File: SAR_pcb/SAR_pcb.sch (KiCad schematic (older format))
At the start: 32 parts, among them J1 Conn_Coaxial_Power, J10 Conn_Coaxial, J2 Conn_Coaxial_Power, J3 Conn_02x10_Top_Bottom, J4 Conn_01x06, J9 Conn_Coaxial, SW1 SW_Push, U2 10B_SAR

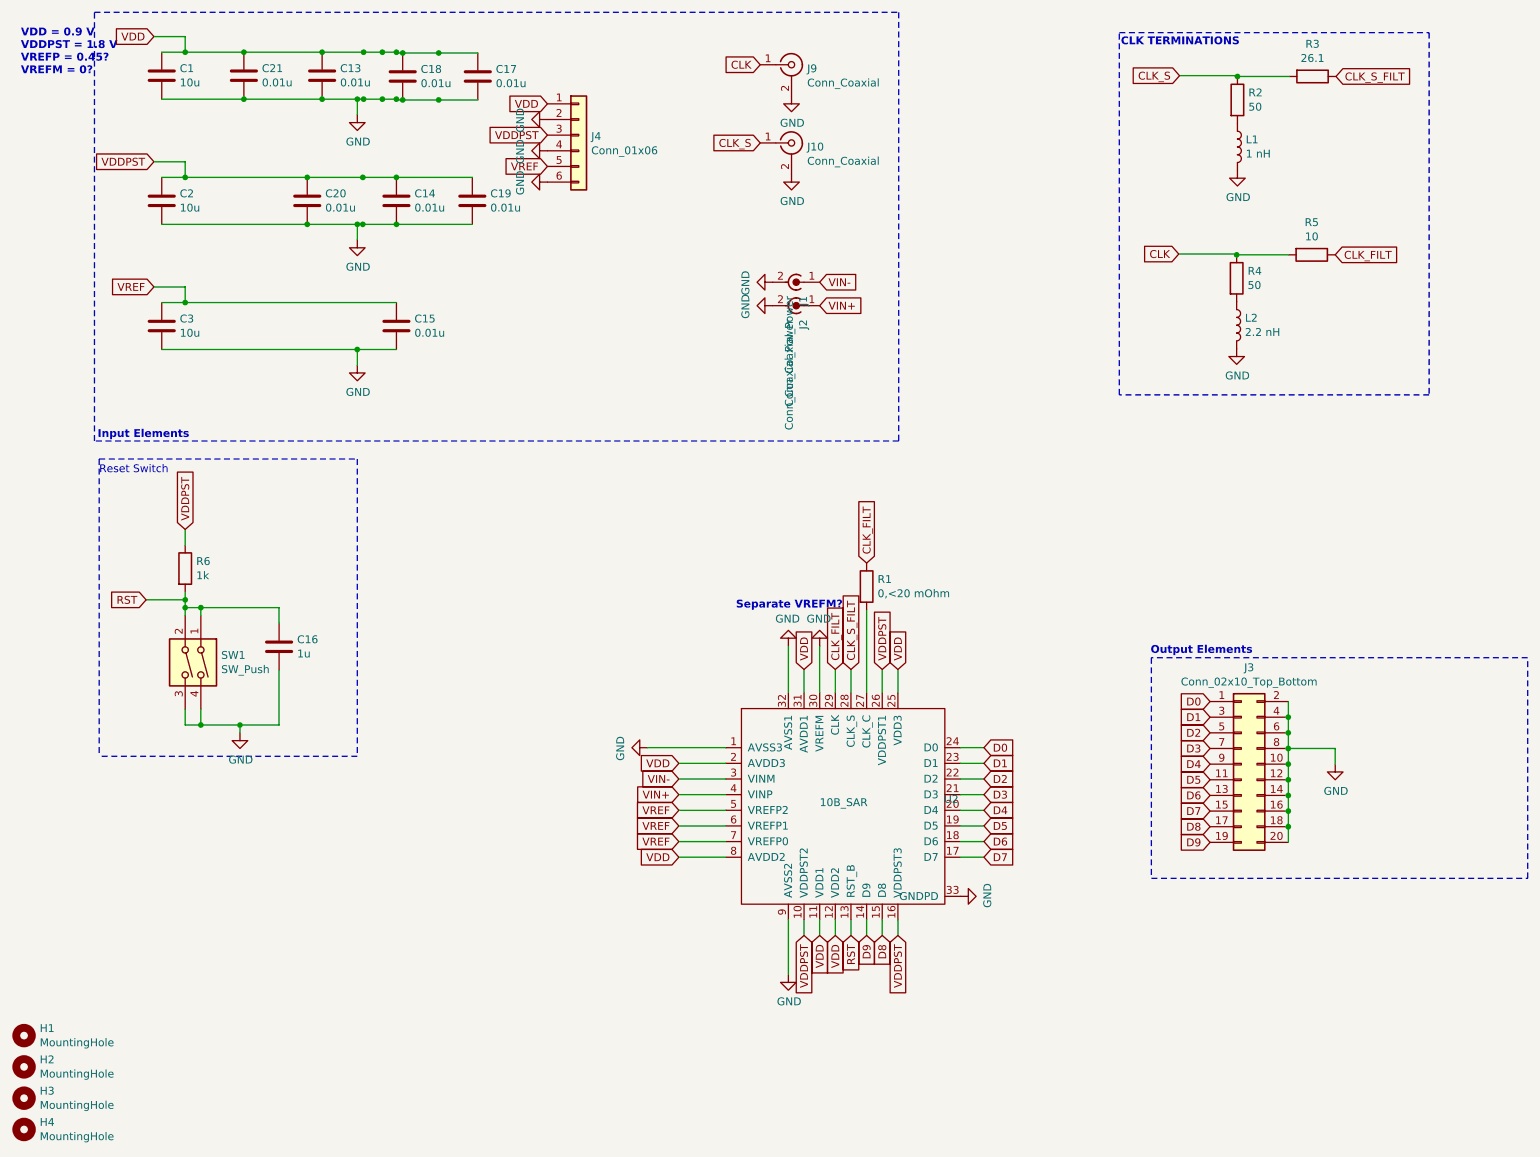
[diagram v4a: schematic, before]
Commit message: Updated BOM for 0603 components
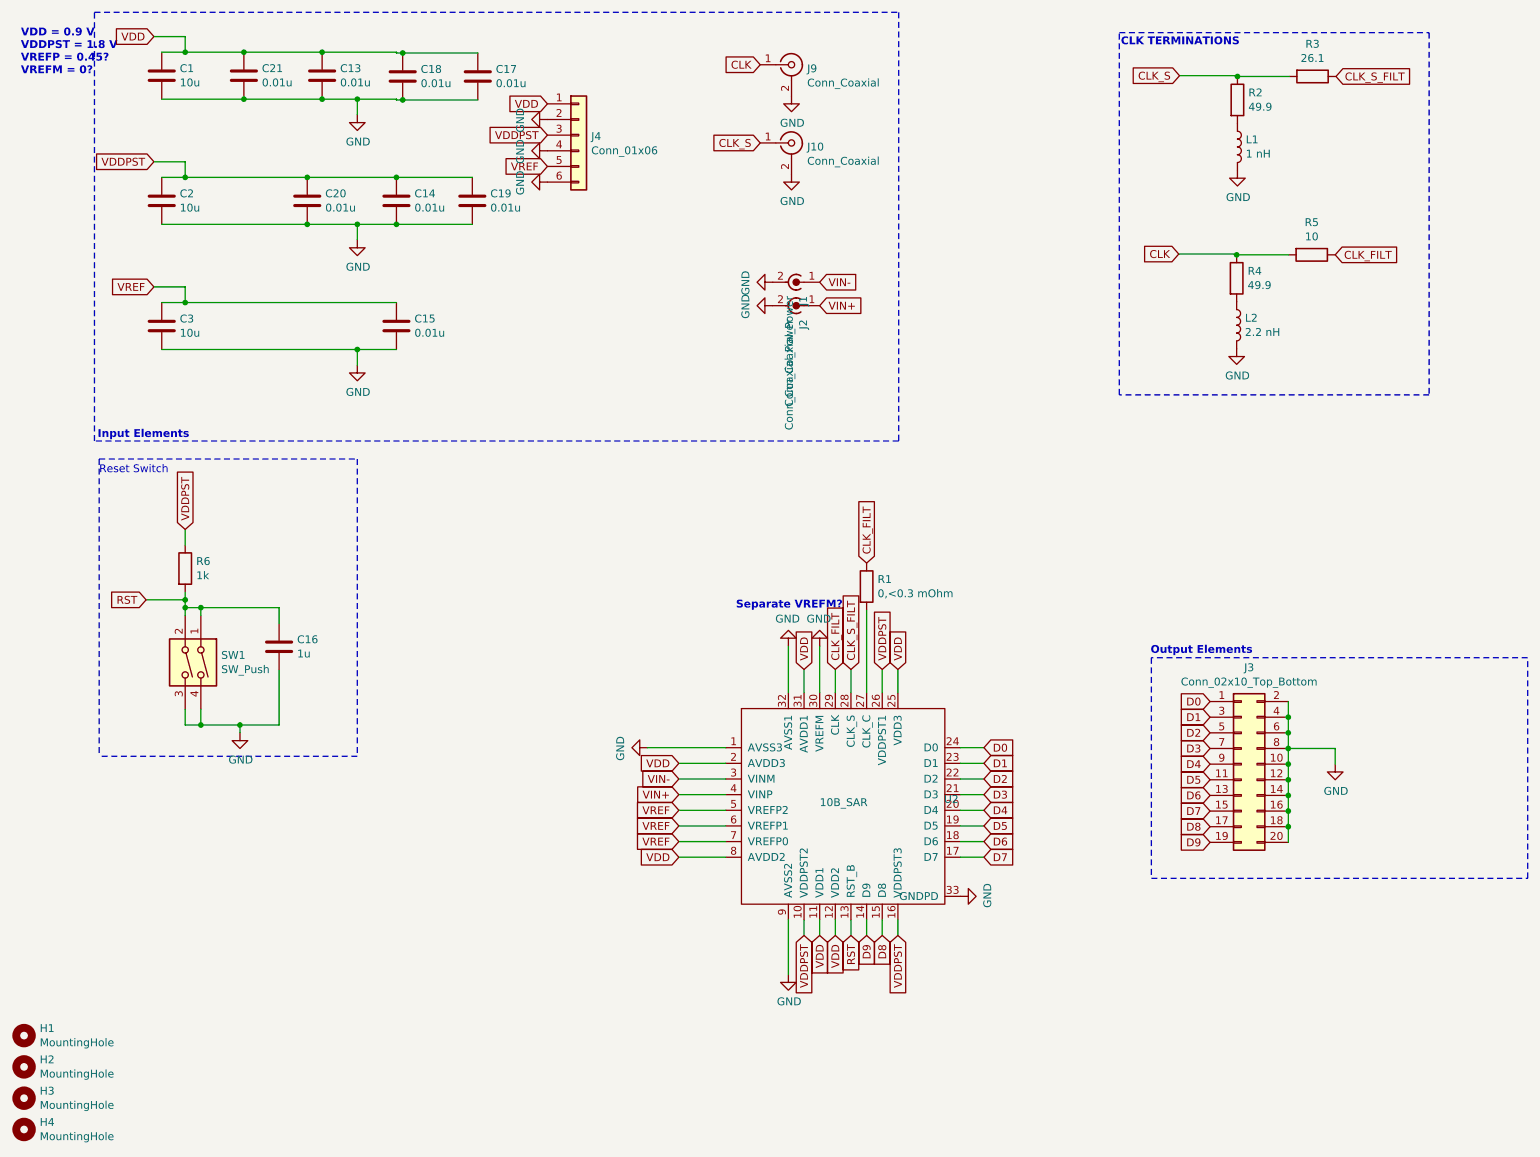
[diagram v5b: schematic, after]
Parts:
- C13, C14, C15, C17, C18, C19, C20, C21: footprint Capacitor_SMD:C_0805_2012Metric -> Capacitor_SMD:C_0603_1608Metric
- L2: footprint Inductor_SMD:L_0805_2012Metric -> Inductor_SMD:L_0603_1608Metric
- R1: value 0,<20 mOhm -> 0,<0.3 mOhm; footprint Resistor_SMD:R_0805_2012Metric -> Resistor_SMD:R_0603_1608Metric
- R2, R4: value 50 -> 49.9; footprint Resistor_SMD:R_0805_2012Metric -> Resistor_SMD:R_0603_1608Metric
- R3, R5: footprint Resistor_SMD:R_0805_2012Metric -> Resistor_SMD:R_0603_1608Metric
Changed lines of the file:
@@
 	2750 1200 2750 1100
 Connection ~ 2750 1100
-Wire Wire Line
-	2750 1100 2790 1100
 $Comp
 L Device:C C14
@@
 F 0 "C14" H 3115 1796 50  0000 L CNN
 F 1 "0.01u" H 3115 1705 50  0000 L CNN
-F 2 "Capacitor_SMD:C_0805_2012Metric" H 3038 1600 50  0001 C CNN
-F 3 "https://www.digikey.com/short/znt40c" H 3000 1750 50  0001 C CNN
+F 2 "Capacitor_SMD:C_0603_1608Metric" H 3038 1600 50  0001 C CNN
+F 3 "https://www.digikey.com/short/znht7p" H 3000 1750 50  0001 C CNN
 	1    3000 1750
 	1    0    0    -1
@@
 	2750 2000 2750 1900
 Connection ~ 2750 1900
-Wire Wire Line
-	2750 1900 2785 1900
 $Comp
 L Device:C C15
@@
 F 0 "C15" H 3115 2596 50  0000 L CNN
 F 1 "0.01u" H 3115 2505 50  0000 L CNN
-F 2 "Capacitor_SMD:C_0805_2012Metric" H 3038 2400 50  0001 C CNN
-F 3 "https://www.digikey.com/short/znt40c" H 3000 2550 50  0001 C CNN
+F 2 "Capacitor_SMD:C_0603_1608Metric" H 3038 2400 50  0001 C CNN
+F 3 "https://www.digikey.com/short/znht7p" H 3000 2550 50  0001 C CNN
 	1    3000 2550
 	1    0    0    -1
@@
 P 6005 4215
 F 0 "R1" H 6075 4261 50  0000 L CNN
-F 1 "0,<20 mOhm" H 6075 4170 50  0000 L CNN
-F 2 "Resistor_SMD:R_0805_2012Metric" V 5935 4215 50  0001 C CNN
-F 3 "https://www.digikey.com/short/znt8qf" H 6005 4215 50  0001 C CNN
+F 1 "0,<0.3 mOhm" H 6075 4170 50  0000 L CNN
+F 2 "Resistor_SMD:R_0603_1608Metric" V 5935 4215 50  0001 C CNN
+F 3 "https://www.digikey.com/short/znhtqv" H 6005 4215 50  0001 C CNN
 	1    6005 4215
 	1    0    0    -1
@@
 P 8375 1105
 F 0 "R2" H 8445 1151 50  0000 L CNN
-F 1 "50" H 8445 1060 50  0000 L CNN
-F 2 "Resistor_SMD:R_0805_2012Metric" V 8305 1105 50  0001 C CNN
-F 3 "https://www.digikey.com/short/zntj08" H 8375 1105 50  0001 C CNN
+F 1 "49.9" H 8445 1060 50  0000 L CNN
+F 2 "Resistor_SMD:R_0603_1608Metric" V 8305 1105 50  0001 C CNN
+F 3 "https://www.digikey.com/short/znht5c" H 8375 1105 50  0001 C CNN
 	1    8375 1105
 	1    0    0    -1
@@
 F 0 "R3" V 8648 955 50  0000 C CNN
 F 1 "26.1" V 8739 955 50  0000 C CNN
-F 2 "Resistor_SMD:R_0805_2012Metric" V 8785 955 50  0001 C CNN
-F 3 "https://www.digikey.com/short/zntpcc" H 8855 955 50  0001 C CNN
+F 2 "Resistor_SMD:R_0603_1608Metric" V 8785 955 50  0001 C CNN
+F 3 "https://www.digikey.com/short/znht2d" H 8855 955 50  0001 C CNN
 	1    8855 955
 	0    1    1    0
@@
 P 8370 2245
 F 0 "R4" H 8440 2291 50  0000 L CNN
-F 1 "50" H 8440 2200 50  0000 L CNN
-F 2 "Resistor_SMD:R_0805_2012Metric" V 8300 2245 50  0001 C CNN
-F 3 "https://www.digikey.com/short/zntj08" H 8370 2245 50  0001 C CNN
+F 1 "49.9" H 8440 2200 50  0000 L CNN
+F 2 "Resistor_SMD:R_0603_1608Metric" V 8300 2245 50  0001 C CNN
+F 3 "https://www.digikey.com/short/znht5c" H 8370 2245 50  0001 C CNN
 	1    8370 2245
 	1    0    0    -1
@@
 F 0 "L2" H 8423 2591 50  0000 L CNN
 F 1 "2.2 nH" H 8423 2500 50  0000 L CNN
-F 2 "Inductor_SMD:L_0805_2012Metric" H 8370 2545 50  0001 C CNN
-F 3 "https://www.digikey.com/short/zntz8b" H 8370 2545 50  0001 C CNN
+F 2 "Inductor_SMD:L_0603_1608Metric" H 8370 2545 50  0001 C CNN
+F 3 "https://www.digikey.com/short/znhtd8" H 8370 2545 50  0001 C CNN
 	1    8370 2545
 	1    0    0    -1
@@
 F 0 "R5" V 8643 2095 50  0000 C CNN
 F 1 "10" V 8734 2095 50  0000 C CNN
-F 2 "Resistor_SMD:R_0805_2012Metric" V 8780 2095 50  0001 C CNN
-F 3 "https://www.digikey.com/short/zntz9r" H 8850 2095 50  0001 C CNN
+F 2 "Resistor_SMD:R_0603_1608Metric" V 8780 2095 50  0001 C CNN
+F 3 "https://www.digikey.com/short/znhtrd" H 8850 2095 50  0001 C CNN
 	1    8850 2095
 	0    1    1    0
@@
 F 0 "C17" H 3635 1001 50  0000 L CNN
 F 1 "0.01u" H 3635 910 50  0000 L CNN
-F 2 "Capacitor_SMD:C_0805_2012Metric" H 3558 805 50  0001 C CNN
-F 3 "https://www.digikey.com/short/znt40c" H 3520 955 50  0001 C CNN
+F 2 "Capacitor_SMD:C_0603_1608Metric" H 3558 805 50  0001 C CNN
+F 3 "https://www.digikey.com/short/znht7p" H 3520 955 50  0001 C CNN
 	1    3520 955
 	1    0    0    -1
 $EndComp
 Wire Wire Line
-	3520 805  3270 805
-Wire Wire Line
 	3000 805  3000 800
-Connection ~ 3000 800
-Wire Wire Line
-	3520 1105 3270 1105
 Wire Wire Line
 	3000 1105 3000 1100
-Connection ~ 3000 1100
 $Comp
 L Device:C C19
@@
 F 0 "C19" H 3600 1796 50  0000 L CNN
 F 1 "0.01u" H 3600 1705 50  0000 L CNN
-F 2 "Capacitor_SMD:C_0805_2012Metric" H 3523 1600 50  0001 C CNN
-F 3 "https://www.digikey.com/short/znt40c" H 3485 1750 50  0001 C CNN
+F 2 "Capacitor_SMD:C_0603_1608Metric" H 3523 1600 50  0001 C CNN
+F 3 "https://www.digikey.com/short/znht7p" H 3485 1750 50  0001 C CNN
 	1    3485 1750
 	1    0    0    -1
@@
 F 0 "C18" H 3155 1001 50  0000 L CNN
 F 1 "0.01u" H 3155 910 50  0000 L CNN
-F 2 "Capacitor_SMD:C_0805_2012Metric" H 3078 805 50  0001 C CNN
-F 3 "https://www.digikey.com/short/znt40c" H 3040 955 50  0001 C CNN
+F 2 "Capacitor_SMD:C_0603_1608Metric" H 3078 805 50  0001 C CNN
+F 3 "https://www.digikey.com/short/znht7p" H 3040 955 50  0001 C CNN
 	1    3040 955
 	1    0    0    -1
 $EndComp
-Connection ~ 3270 805
-Wire Wire Line
-	3270 805  3040 805
-Connection ~ 3270 1105
-Wire Wire Line
-	3270 1105 3040 1105
 $Comp
 L Device:C C21
@@
 F 0 "C21" H 2140 996 50  0000 L CNN
 F 1 "0.01u" H 2140 905 50  0000 L CNN
-F 2 "Capacitor_SMD:C_0805_2012Metric" H 2063 800 50  0001 C CNN
-F 3 "https://www.digikey.com/short/znt40c" H 2025 950 50  0001 C CNN
+F 2 "Capacitor_SMD:C_0603_1608Metric" H 2063 800 50  0001 C CNN
+F 3 "https://www.digikey.com/short/znht7p" H 2025 950 50  0001 C CNN
 	1    2025 950
 	1    0    0    -1
 $EndComp
-Connection ~ 2790 800
-Wire Wire Line
-	2790 800  2910 800
-Connection ~ 2790 1100
-Wire Wire Line
-	2790 1100 2910 1100
 $Comp
 L Device:C C20
@@
 F 0 "C20" H 2545 1796 50  0000 L CNN
 F 1 "0.01u" H 2545 1705 50  0000 L CNN
-F 2 "Capacitor_SMD:C_0805_2012Metric" H 2468 1600 50  0001 C CNN
-F 3 "https://www.digikey.com/short/znt40c" H 2430 1750 50  0001 C CNN
+F 2 "Capacitor_SMD:C_0603_1608Metric" H 2468 1600 50  0001 C CNN
+F 3 "https://www.digikey.com/short/znht7p" H 2430 1750 50  0001 C CNN
 	1    2430 1750
 	1    0    0    -1
 $EndComp
-Connection ~ 2785 1600
-Wire Wire Line
-	2785 1600 3000 1600
-Connection ~ 2785 1900
-Wire Wire Line
-	2785 1900 3000 1900
 Wire Wire Line
 	1650 800  2025 800
@@
 	1500 2700 2750 2700
 Connection ~ 2430 1600
-Wire Wire Line
-	2430 1600 2785 1600
 Connection ~ 2430 1900
 Wire Wire Line
@@
 F 0 "C13" H 2640 996 50  0000 L CNN
 F 1 "0.01u" H 2640 905 50  0000 L CNN
-F 2 "Capacitor_SMD:C_0805_2012Metric" H 2563 800 50  0001 C CNN
-F 3 "https://www.digikey.com/short/znt40c" H 2525 950 50  0001 C CNN
+F 2 "Capacitor_SMD:C_0603_1608Metric" H 2563 800 50  0001 C CNN
+F 3 "https://www.digikey.com/short/znht7p" H 2525 950 50  0001 C CNN
 	1    2525 950
 	1    0    0    -1
 $EndComp
 Connection ~ 2525 800
-Wire Wire Line
-	2525 800  2790 800
 Connection ~ 2525 1100
 Wire Wire Line
 	2525 1100 2750 1100
-Connection ~ 2910 800
-Wire Wire Line
-	2910 800  3000 800
-Connection ~ 2910 1100
-Wire Wire Line
-	2910 1100 3000 1100
 Connection ~ 3040 805
 Wire Wire Line
@@
 Wire Wire Line
 	3040 1105 3000 1105
+Wire Wire Line
+	2750 1900 3000 1900
+Wire Wire Line
+	3040 805  3520 805
+Wire Wire Line
+	3040 1105 3520 1105
+Wire Wire Line
+	2430 1600 3000 1600
+Wire Wire Line
+	2525 800  3000 800
+Wire Wire Line
+	2750 1100 3000 1100
 $EndSCHEMATC

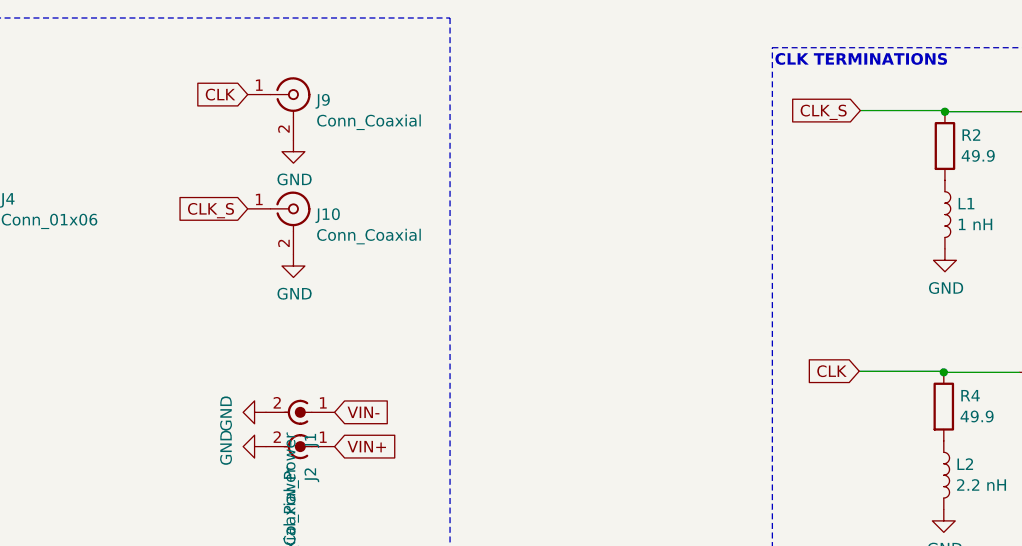
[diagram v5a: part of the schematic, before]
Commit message: Updated PCB to conform to Vanessa's recommendations
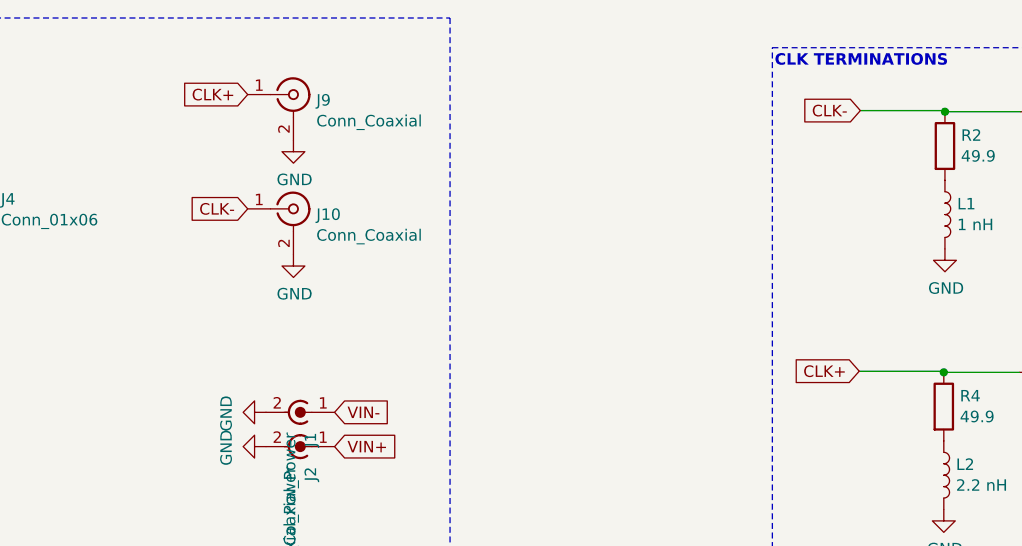
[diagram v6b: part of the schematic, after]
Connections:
- net CLK renamed CLK+
- net CLK_S renamed CLK-
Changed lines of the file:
@@
 	1    0    0    -1
 $EndComp
-Text GLabel 5325 1380 0    50   Input ~ 0
-CLK_S
 Text GLabel 5325 880  0    50   Input ~ 0
-CLK
+CLK+
 $Comp
 L Device:C C1
@@
 	6005 4365 6005 4895
 Text GLabel 8005 950  0    50   Input ~ 0
-CLK_S
+CLK-
 $Comp
 L Device:R R2
@@
 Output Elements
 Text GLabel 8000 2090 0    50   Input ~ 0
-CLK
+CLK+
 $Comp
 L Device:R R4
@@
 Wire Wire Line
 	2750 1100 3000 1100
+Text GLabel 5325 1380 0    50   Input ~ 0
+CLK-
 $EndSCHEMATC

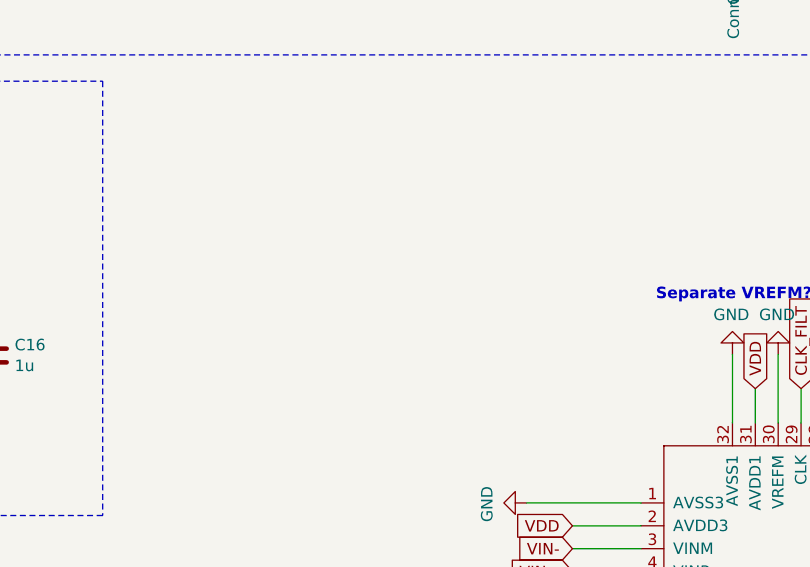
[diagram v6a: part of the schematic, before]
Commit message: Added input termination
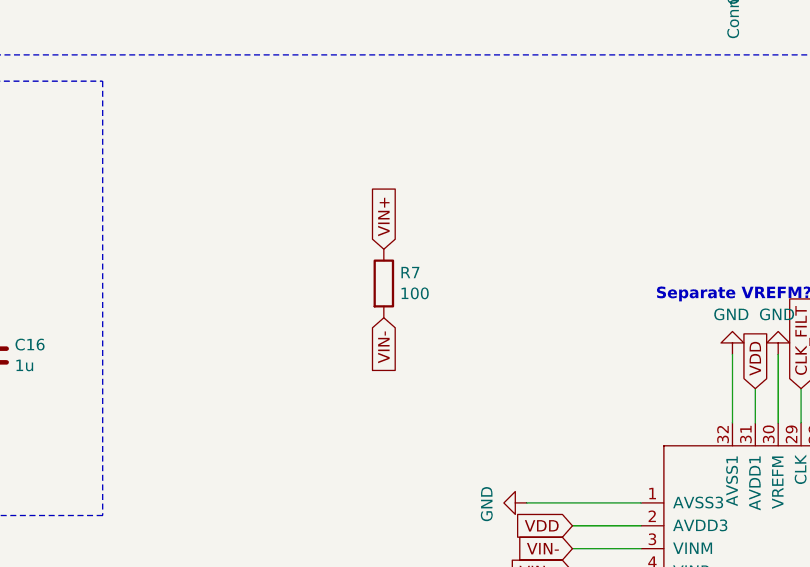
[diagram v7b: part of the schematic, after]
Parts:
- added R7: 100, Resistor_SMD:R_0603_1608Metric, symbol Device:R
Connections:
- net VIN+: now also R7.1
- net VIN-: now also R7.2
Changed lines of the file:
@@
 Text GLabel 5325 1380 0    50   Input ~ 0
 CLK-
+$Comp
+L Device:R R7
+U 1 1 5F8D1B9C
+P 3980 4285
+F 0 "R7" H 4050 4331 50  0000 L CNN
+F 1 "100" H 4050 4240 50  0000 L CNN
+F 2 "Resistor_SMD:R_0603_1608Metric" V 3910 4285 50  0001 C CNN
+F 3 "https://www.digikey.com/short/znhvnf" H 3980 4285 50  0001 C CNN
+	1    3980 4285
+	1    0    0    -1
+$EndComp
+Text GLabel 3980 4435 3    50   Input ~ 0
+VIN-
+Text GLabel 3980 4135 1    50   Input ~ 0
+VIN+
 $EndSCHEMATC
